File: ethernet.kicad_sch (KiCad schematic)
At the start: 37 parts, among them J801 SI-60062-F, U801 LAN8742A-CZ-TR, U802 USBLC6-4SC6, Y801 Crystal_GND24

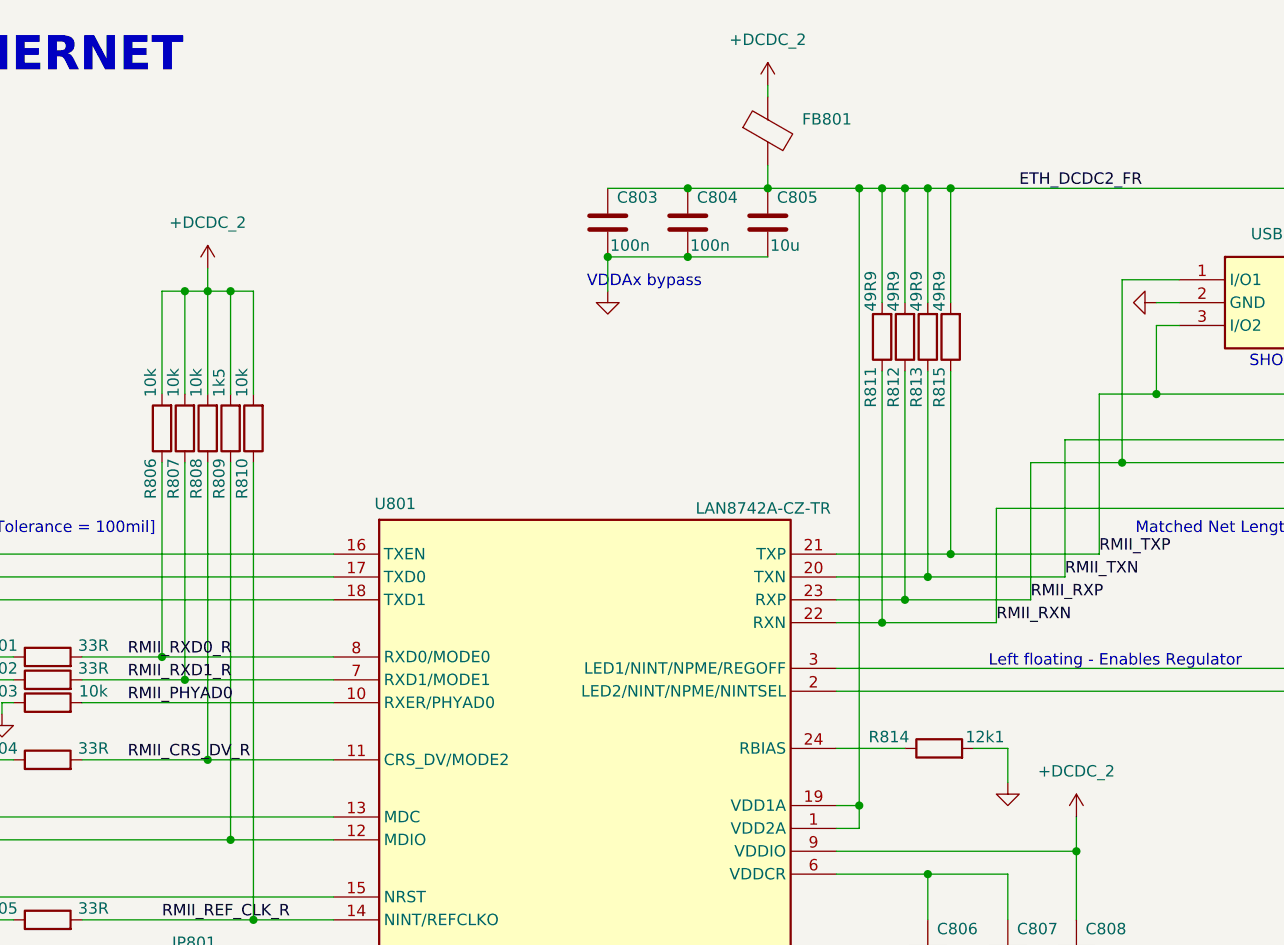
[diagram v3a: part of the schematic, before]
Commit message: validation BOM
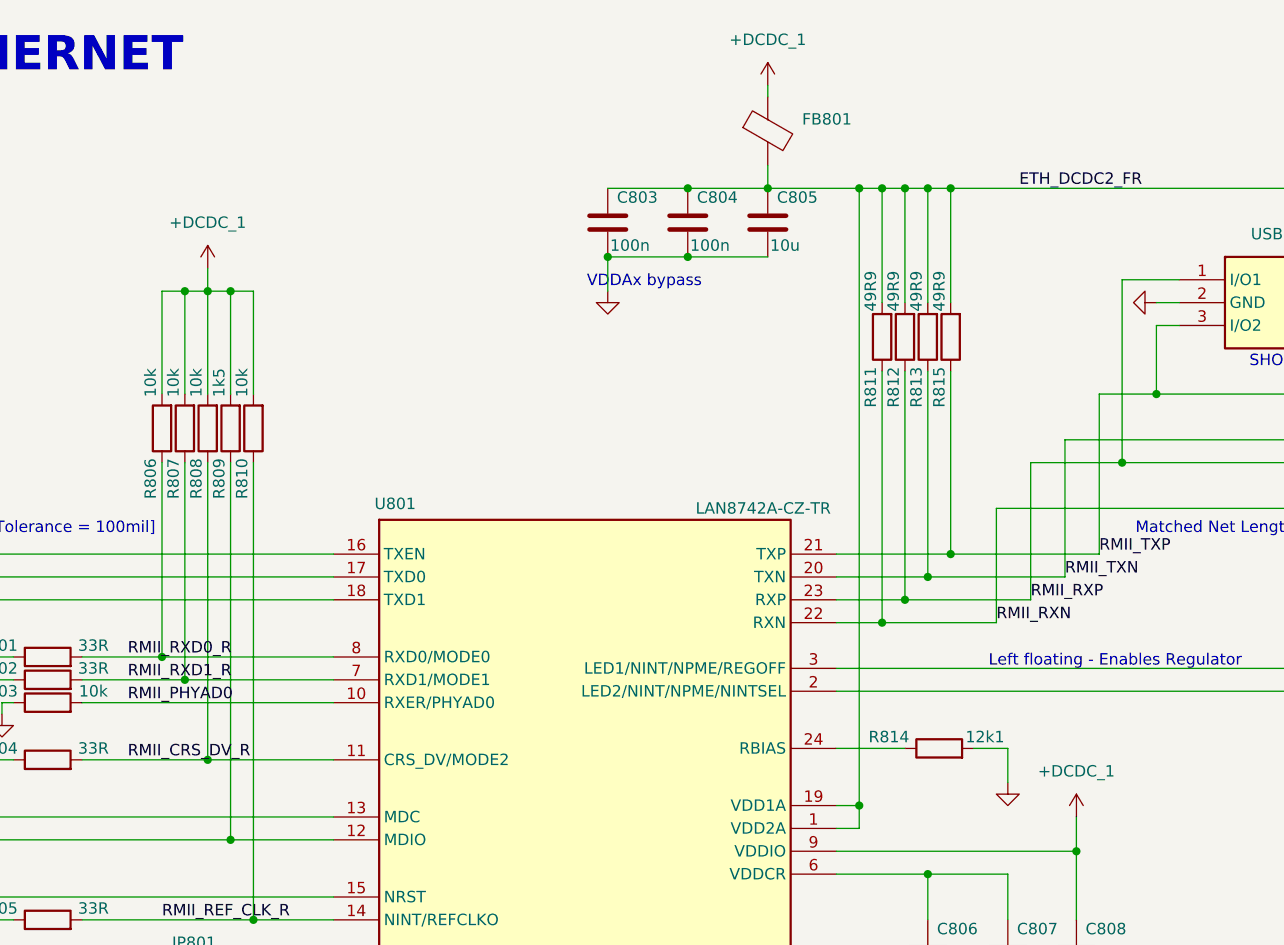
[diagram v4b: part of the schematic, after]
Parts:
- C807: Manufacturer_Name KYOCERA AVX -> KYOCERA AVX
- C812: Distributor_Link https://www.mouser.com/ProductDetail/Murata-Electronics/GCM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 -> https://www.mouser.com/ProductDetail/KYOCERA-AVX/04025C102K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; Manufacturer_Name Murata Electronics -> KYOCERA AVX; Manufacturer_Part_Number GCM1555C2A102JE02D -> 04025C102KAZ2A
- J801: Distributor_Link (none) -> https://www.mouser.com/ProductDetail/Bel-Magnetic-Solutions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
- R818, R819: Distributor_Link https://www.mouser.com/ProductDetail/YAGEO/TR0603NR-07270RL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 -> https://www.mouser.com/ProductDetail/TE-Connectivity-Holswo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; Manufacturer_Name YAGEO -> TE Connectivity; Manufacturer_Part_Number TR0603NR-07270RL -> CRGH0603F270R
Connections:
- net +DCDC_2 renamed +DCDC_1
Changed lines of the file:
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@@
 			)
 		)
-		(property "Datasheet" "https://www.mouser.com/datasheet/3/76/1/GCM1555C2A102JE02-01A.pdf"
+		(property "Datasheet" "https://datasheets.kyocera-avx.com/X7RDielectric.pdf"
 			(at 256.54 52.07 0)
 			(effects
@@
 			)
 		)
-		(property "Distributor_Link" "https://www.mouser.com/ProductDetail/Murata-Electronics/GCM1555C2A102JE02D?qs=ZcfC38r4PotRVMCtISugCA%3D%3D"
+		(property "Distributor_Link" "https://www.mouser.com/ProductDetail/KYOCERA-AVX/04025C102KAZ2A?qs=%252BdQmOuGyFcHUWKrsS7iuyw%3D%3D"
 			(at 256.54 52.07 0)
 			(effects
@@
 			)
 		)
-		(property "Manufacturer_Name" "Murata Electronics"
+		(property "Manufacturer_Name" "KYOCERA AVX "
 			(at 256.54 52.07 0)
 			(effects
@@
 			)
 		)
-		(property "Manufacturer_Part_Number" "GCM1555C2A102JE02D"
+		(property "Manufacturer_Part_Number" "04025C102KAZ2A"
 			(at 256.54 52.07 0)
 			(effects
@@
 	)
 	(symbol
-		(lib_id "EMS:+DCDC_2")
-		(at 154.94 104.14 0)
-		(unit 1)
-		(exclude_from_sim no)
-		(in_bom no)
-		(on_board no)
-		(dnp no)
-		(fields_autoplaced yes)
-		(property "Reference" "#PWR0811"
-			(at 154.94 104.14 0)
-			(effects
-				(font
-					(size 1.27 1.27)
-				)
-				(hide yes)
-			)
-		)
-		(property "Value" "+DCDC_2"
-			(at 154.94 99.06 0)
-			(effects
-				(font
-					(size 1.27 1.27)
-				)
-			)
-		)
-		(property "Footprint" ""
-			(at 154.94 104.14 0)
-			(effects
-				(font
-					(size 1.27 1.27)
-				)
-				(hide yes)
-			)
-		)
-		(property "Datasheet" ""
-			(at 154.94 104.14 0)
-			(effects
-				(font
-					(size 1.27 1.27)
-				)
-				(hide yes)
-			)
-		)
-		(property "Description" "Power symbol for \"+DCDC_2V\""
-			(at 155.702 113.03 0)
-			(effects
-				(font
-					(size 1.27 1.27)
-				)
-				(hide yes)
-			)
-		)
-		(pin "1"
-		)
-		(instances
-			(project "EnergyMonitoringSystem"
-				(path "/e660428c-c9b7-476c-8ac8-2d419f233469/226bef4b-1d5d-48eb-b4d8-e2f18f5b1a03"
-					(reference "#PWR0811")
-					(unit 1)
-				)
-			)
-		)
-	)
-	(symbol
 		(lib_id "power:GND")
 		(at 218.44 50.8 0)
@@
 	)
 	(symbol
-		(lib_id "EMS:+DCDC_2")
+		(lib_id "EMS:+DCDC_1")
 		(at 120.65 22.86 0)
 		(unit 1)
@@
 		(dnp no)
 		(fields_autoplaced yes)
-		(property "Reference" "#PWR0808"
-			(at 120.65 22.86 0)
+		(property "Reference" "#PWR0805"
+			(at 125.984 20.32 0)
 			(effects
 				(font
@@
 			)
 		)
-		(property "Value" "+DCDC_2"
+		(property "Value" "+DCDC_1"
 			(at 120.65 17.78 0)
 			(effects
@@
 			)
 		)
-		(property "Description" "Power symbol for \"+DCDC_2V\""
-			(at 121.412 31.75 0)
+		(property "Description" "Power supply \"+DCDC_1V\""
+			(at 120.904 33.274 0)
 			(effects
 				(font
@@
 			(project "EnergyMonitoringSystem"
 				(path "/e660428c-c9b7-476c-8ac8-2d419f233469/226bef4b-1d5d-48eb-b4d8-e2f18f5b1a03"
-					(reference "#PWR0808")
+					(reference "#PWR0805")
+					(unit 1)
+				)
+			)
+		)
+	)
+	(symbol
+		(lib_id "EMS:+DCDC_1")
+		(at 58.42 43.18 0)
+		(unit 1)
+		(exclude_from_sim no)
+		(in_bom no)
+		(on_board no)
+		(dnp no)
+		(fields_autoplaced yes)
+		(property "Reference" "#PWR0818"
+			(at 63.754 40.64 0)
+			(effects
+				(font
+					(size 1.27 1.27)
+				)
+				(hide yes)
+			)
+		)
+		(property "Value" "+DCDC_1"
+			(at 58.42 38.1 0)
+			(effects
+				(font
+					(size 1.27 1.27)
+				)
+			)
+		)
+		(property "Footprint" ""
+			(at 58.42 43.18 0)
+			(effects
+				(font
+					(size 1.27 1.27)
+				)
+				(hide yes)
+			)
+		)
+		(property "Datasheet" ""
+			(at 58.42 43.18 0)
+			(effects
+				(font
+					(size 1.27 1.27)
+				)
+				(hide yes)
+			)
+		)
+		(property "Description" "Power supply \"+DCDC_1V\""
+			(at 58.674 53.594 0)
+			(effects
+				(font
+					(size 1.27 1.27)
+				)
+				(hide yes)
+			)
+		)
+		(pin "1"
+		)
+		(instances
+			(project "EnergyMonitoringSystem"
+				(path "/e660428c-c9b7-476c-8ac8-2d419f233469/226bef4b-1d5d-48eb-b4d8-e2f18f5b1a03"
+					(reference "#PWR0818")
 					(unit 1)
 				)
@@
 			)
 		)
-		(property "Manufacturer_Name" "KYOCERA AVX"
+		(property "Manufacturer_Name" "KYOCERA AVX "
 			(at 147.32 119.38 0)
 			(effects
@@
 			)
 		)
+		(property "Distributor_Link" "https://www.mouser.com/ProductDetail/Bel-Magnetic-Solutions/SI-60062-F?qs=FESYatJ8odK8fgoNWoNb9g%3D%3D"
+			(at 213.36 57.15 0)
+			(effects
+				(font
+					(size 1.27 1.27)
+				)
+				(hide yes)
+			)
+		)
 		(pin "6"
 		)
@@
 	)
 	(symbol
-		(lib_id "EMS:+DCDC_2")
-		(at 58.42 43.18 0)
+		(lib_id "EMS:+DCDC_1")
+		(at 154.94 104.14 0)
 		(unit 1)
 		(exclude_from_sim no)
@@
 		(dnp no)
 		(fields_autoplaced yes)
-		(property "Reference" "#PWR0805"
-			(at 58.42 43.18 0)
+		(property "Reference" "#PWR0808"
+			(at 160.274 101.6 0)
 			(effects
 				(font
@@
 			)
 		)
-		(property "Value" "+DCDC_2"
-			(at 58.42 38.1 0)
+		(property "Value" "+DCDC_1"
+			(at 154.94 99.06 0)
 			(effects
 				(font
@@
 		)
 		(property "Footprint" ""
-			(at 58.42 43.18 0)
+			(at 154.94 104.14 0)
 			(effects
 				(font
@@
 		)
 		(property "Datasheet" ""
-			(at 58.42 43.18 0)
+			(at 154.94 104.14 0)
 			(effects
 				(font
@@
 			)
 		)
-		(property "Description" "Power symbol for \"+DCDC_2V\""
-			(at 59.182 52.07 0)
+		(property "Description" "Power supply \"+DCDC_1V\""
+			(at 155.194 114.554 0)
 			(effects
 				(font
@@
 			(project "EnergyMonitoringSystem"
 				(path "/e660428c-c9b7-476c-8ac8-2d419f233469/226bef4b-1d5d-48eb-b4d8-e2f18f5b1a03"
-					(reference "#PWR0805")
+					(reference "#PWR0808")
 					(unit 1)
 				)
@@
 			)
 		)
-		(property "Datasheet" "https://www.mouser.com/datasheet/3/508/1/PYu-TR_0-30_RoHS_L_1.pdf"
+		(property "Datasheet" "https://www.te.com/commerce/DocumentDelivery/DDEController?Action=srchrtrv&DocNm=1773204-1&DocType=Data%20Sheet&DocLang=English&PartCntxt=2176177-4&DocFormat=pdf"
 			(at 262.89 86.36 0)
 			(effects
@@
 			)
 		)
-		(property "Distributor_Link" "https://www.mouser.com/ProductDetail/YAGEO/TR0603NR-07270RL?qs=k2KEx2DUIRRrefrp4eQOhw%3D%3D"
+		(property "Distributor_Link" "https://www.mouser.com/ProductDetail/TE-Connectivity-Holsworthy/CRGH0603F270R?qs=gt1LBUVyoHkSOaKreGSGBQ%3D%3D"
 			(at 262.89 86.36 0)
 			(effects
@@
 			)
 		)
-		(property "Manufacturer_Name" "YAGEO"
+		(property "Manufacturer_Name" "TE Connectivity"
 			(at 262.89 86.36 0)
 			(effects
@@
 			)
 		)
-		(property "Manufacturer_Part_Number" "TR0603NR-07270RL"
+		(property "Manufacturer_Part_Number" "CRGH0603F270R"
 			(at 262.89 86.36 0)
 			(effects
@@
 			)
 		)
-		(property "Datasheet" "https://www.mouser.com/datasheet/3/508/1/PYu-TR_0-30_RoHS_L_1.pdf"
+		(property "Datasheet" "https://www.te.com/commerce/DocumentDelivery/DDEController?Action=srchrtrv&DocNm=1773204-1&DocType=Data%20Sheet&DocLang=English&PartCntxt=2176177-4&DocFormat=pdf"
 			(at 267.97 86.36 0)
 			(effects
@@
 			)
 		)
-		(property "Distributor_Link" "https://www.mouser.com/ProductDetail/YAGEO/TR0603NR-07270RL?qs=k2KEx2DUIRRrefrp4eQOhw%3D%3D"
+		(property "Distributor_Link" "https://www.mouser.com/ProductDetail/TE-Connectivity-Holsworthy/CRGH0603F270R?qs=gt1LBUVyoHkSOaKreGSGBQ%3D%3D"
 			(at 267.97 86.36 0)
 			(effects
@@
 			)
 		)
-		(property "Manufacturer_Name" "YAGEO"
+		(property "Manufacturer_Name" "TE Connectivity"
 			(at 267.97 86.36 0)
 			(effects
@@
 			)
 		)
-		(property "Manufacturer_Part_Number" "TR0603NR-07270RL"
+		(property "Manufacturer_Part_Number" "CRGH0603F270R"
 			(at 267.97 86.36 0)
 			(effects

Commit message: finetune ethernet lines
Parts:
- R801, R802, R804, R805: footprint Resistor_SMD:R_0603_1608Metric -> Resistor_SMD:R_0402_1005Metric; Distributor_Link https://www.mouser.com/ProductDetail/ROHM-Semiconductor/ESR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 -> https://www.mouser.com/ProductDetail/YAGEO/RC0402FR-7D33RL?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; Manufacturer_Name ROHM Semiconductor -> YAGEO; Manufacturer_Part_Number ESR03EZPF33R0 -> RC0402FR-7D33RL
- R803, R806, R807, R808, R810, R816, R817: footprint Resistor_SMD:R_0603_1608Metric -> Resistor_SMD:R_0402_1005Metric; Distributor_Link https://www.mouser.com/ProductDetail/Vishay-Dale/CRCW060310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 -> https://www.mouser.com/ProductDetail/Panasonic/ERJ-PA2F1002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; Manufacturer_Name Vishay/Dale -> Panasonic; Manufacturer_Part_Number CRCW060310K0FKEI -> ERJ-PA2F1002X
- R809: footprint Resistor_SMD:R_0603_1608Metric -> Resistor_SMD:R_0402_1005Metric

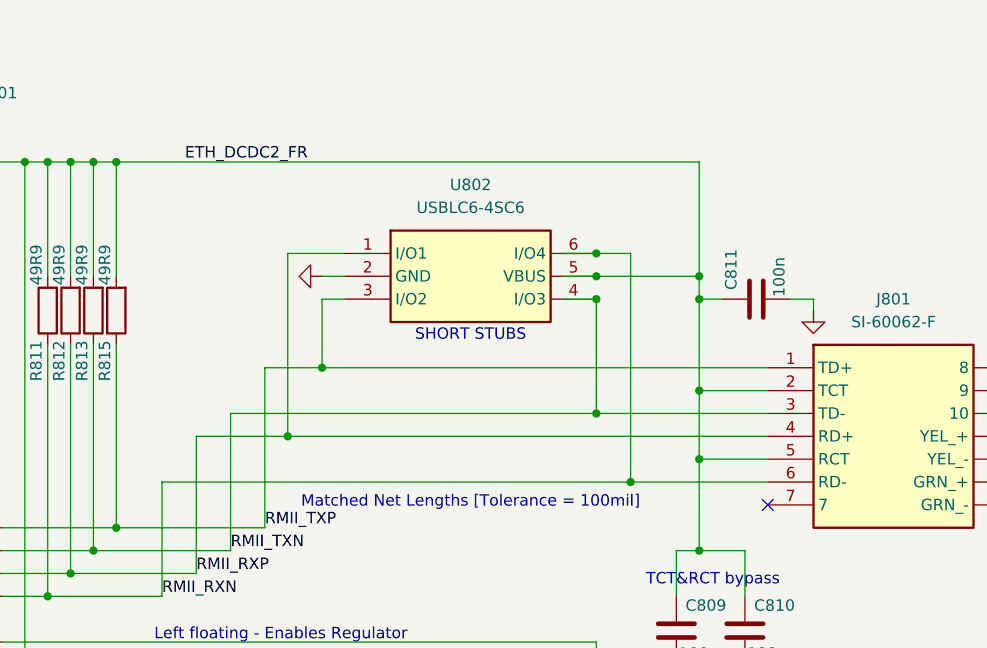
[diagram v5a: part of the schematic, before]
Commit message: fine tune high speed traces
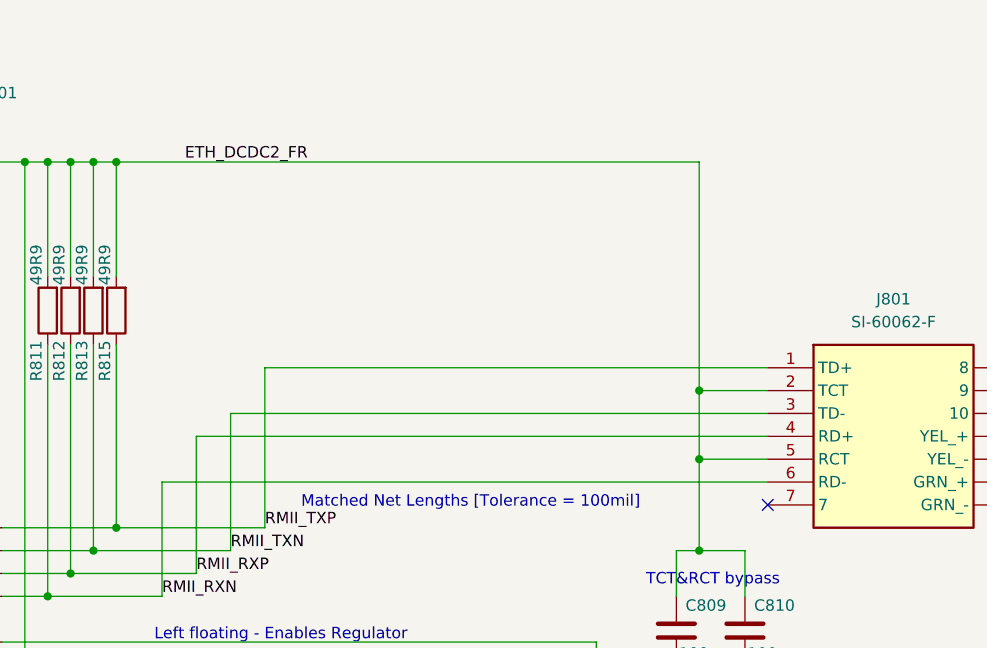
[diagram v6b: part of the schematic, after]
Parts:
- removed C811: 100n, Capacitor_SMD:C_0402_1005Metric, symbol Device:C
- removed U802: USBLC6-4SC6, EMS:USBLC6-4SC6_SOT95-6N, symbol EMS:USBLC6-4SC6
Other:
- note removed: "SHORT STUBS"

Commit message: minor design improvements
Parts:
- removed JP801: SolderJumper_2_Bridged, Jumper:SolderJumper-2_P1.3mm_Bridged_RoundedPad1.0x1.5mm, symbol Jumper:SolderJumper_2_Bridged
- added R820: 0R, Resistor_SMD:R_0603_1608Metric, symbol Device:R
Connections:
- net RMII_XTAL2: now also R820.2
- net at C801.2, Y801.1: now also R820.1
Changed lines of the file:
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@@
 	(wire
 		(pts
+			(xy 60.96 120.65) (xy 72.39 120.65)
+		)
+		(stroke
+			(width 0)
+			(type default)
+		)
+	)
+	(wire
+		(pts
 			(xy 60.96 106.68) (xy 60.96 64.77)
 		)
@@
 	(wire
 		(pts
-			(xy 60.96 120.65) (xy 72.39 120.65)
-		)
-		(stroke
-			(width 0)
-			(type default)
-		)
-	)
-	(wire
-		(pts
 			(xy 140.97 34.29) (xy 140.97 46.99)
 		)
@@
 	)
 	(symbol
-		(lib_id "Jumper:SolderJumper_2_Bridged")
-		(at 57.15 120.65 0)
-		(unit 1)
-		(exclude_from_sim yes)
-		(in_bom no)
-		(on_board yes)
-		(dnp no)
-		(property "Reference" "JP801"
-			(at 56.896 118.11 0)
-			(effects
-				(font
-					(size 1.27 1.27)
-				)
-			)
-		)
-		(property "Value" "SolderJumper_2_Bridged"
-			(at 57.15 116.84 0)
-			(effects
-				(font
-					(size 1.27 1.27)
-				)
-				(hide yes)
-			)
-		)
-		(property "Footprint" "Jumper:SolderJumper-2_P1.3mm_Bridged_RoundedPad1.0x1.5mm"
-			(at 57.15 120.65 0)
-			(effects
-				(font
-					(size 1.27 1.27)
-				)
-				(hide yes)
-			)
-		)
-		(property "Datasheet" "~"
-			(at 57.15 120.65 0)
-			(effects
-				(font
-					(size 1.27 1.27)
-				)
-				(hide yes)
-			)
-		)
-		(property "Description" "Solder Jumper, 2-pole, closed/bridged"
-			(at 57.15 120.65 0)
-			(effects
-				(font
-					(size 1.27 1.27)
-				)
-				(hide yes)
-			)
-		)
-		(pin "1"
-		)
-		(pin "2"
-		)
-		(instances
-			(project "EnergyMonitoringSystem"
-				(path "/e660428c-c9b7-476c-8ac8-2d419f233469/226bef4b-1d5d-48eb-b4d8-e2f18f5b1a03"
-					(reference "JP801")
-					(unit 1)
-				)
-			)
-		)
-	)
-	(symbol
 		(lib_id "Device:C")
 		(at 36.83 120.65 90)
@@
 					(unit 1)
 				)
+			)
+		)
+	)
+	(symbol
+		(lib_id "Device:R")
+		(at 57.15 120.65 90)
+		(unit 1)
+		(exclude_from_sim no)
+		(in_bom yes)
+		(on_board yes)
+		(dnp no)
+		(property "Reference" "R820"
+			(at 50.546 117.856 90)
+			(effects
+				(font
+					(size 1.27 1.27)
+				)
+			)
+		)
+		(property "Value" "0R"
+			(at 57.404 117.856 90)
+			(effects
+				(font
+					(size 1.27 1.27)
+				)
+			)
+		)
+		(property "Footprint" "Resistor_SMD:R_0603_1608Metric"
+			(at 57.15 122.428 90)
+			(effects
+				(font
+					(size 1.27 1.27)
+				)
+				(hide yes)
+			)
+		)
+		(property "Datasheet" "https://www.vishay.com/doc?20035https://www.vishay.com/doc?20035"
+			(at 57.15 120.65 0)
+			(effects
+				(font
+					(size 1.27 1.27)
+				)
+				(hide yes)
+			)
+		)
+		(property "Description" "Resistor"
+			(at 57.15 120.65 0)
+			(effects
+				(font
+					(size 1.27 1.27)
+				)
+				(hide yes)
+			)
+		)
+		(property "Distributor_Link" "https://www.mouser.com/ProductDetail/Vishay/CRCW06030000Z0EI?qs=%252B6g0mu59x7L7KQG%252Bwwt0jQ%3D%3D"
+			(at 57.15 120.65 0)
+			(effects
+				(font
+					(size 1.27 1.27)
+				)
+				(hide yes)
+			)
+		)
+		(property "Manufacturer_Name" "Vishay"
+			(at 57.15 120.65 0)
+			(effects
+				(font
+					(size 1.27 1.27)
+				)
+				(hide yes)
+			)
+		)
+		(property "Manufacturer_Part_Number" "CRCW06030000Z0EI"
+			(at 57.15 120.65 0)
+			(effects
+				(font
+					(size 1.27 1.27)
+				)
+				(hide yes)
+			)
+		)
+		(pin "2"
+		)
+		(pin "1"
+		)
+		(instances
+			(project "EnergyMonitoringSystem"
+				(path "/e660428c-c9b7-476c-8ac8-2d419f233469/226bef4b-1d5d-48eb-b4d8-e2f18f5b1a03"
+					(reference "R820")
+					(unit 1)
+				)
